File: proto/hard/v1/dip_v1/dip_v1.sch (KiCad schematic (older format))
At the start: 74 parts, among them J1 RJ12, J10 Conn_01x04_Female, J11 Conn_01x02_Male, J12 Conn_01x04_Female, J13 Conn_01x09_Male, J14 Conn_02x02_Counter_Clockwise, J2 RJ12, J3 RJ12, J4 RJ12, J5 Conn_01x04_Female, J6 RJ45, J7 AudioJack3, J8 Conn_01x04_Female, J9 Conn_01x05_Male, Q1 2N7000, Q2 2N7000, Q3 2N7000, Q4 BS250, Q5 BS250, Q6 2N7000, Q7 BS250, U1 BluePill, U2 LM339, U3 ST485EBDR, U4 74HC595, U5 ULN2803A, U6 74HC04, U7 LM358

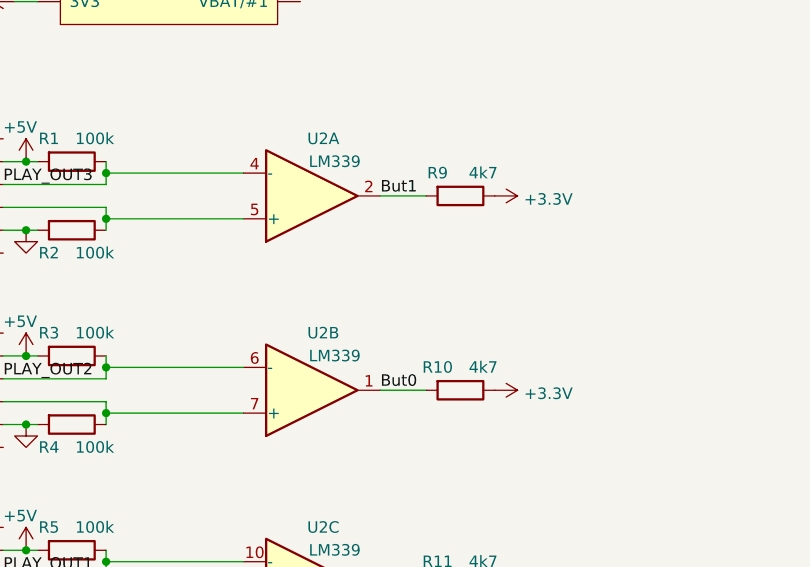
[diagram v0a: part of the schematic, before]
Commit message: Added example project with button connection schematic only. Corrected "dip" pins assignment to comply with main project.
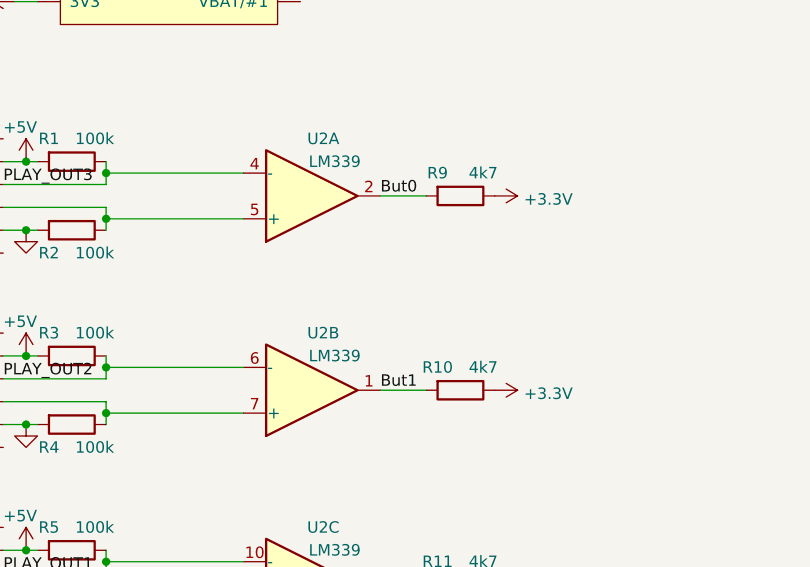
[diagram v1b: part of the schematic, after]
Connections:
- net But0: now also R9.2, U2.2; no longer R10.2, U2.1
- net But1: now also R10.2, U2.1; no longer R9.2, U2.2
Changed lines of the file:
@@
 EESchema Schematic File Version 4
-LIBS:dip_v1-cache
 EELAYER 29 0
 EELAYER END
@@
 Wire Wire Line
 	1900 3650 1900 3700
-Text Label 3100 3550 0    50   ~ 0
+Text Label 3100 4400 0    50   ~ 0
 But1
 Text Label 3100 5250 0    50   ~ 0
@@
 Text Label 3100 6100 0    50   ~ 0
 But3
-Text Label 3100 4400 0    50   ~ 0
+Text Label 3100 3550 0    50   ~ 0
 But0
 Text Label 1600 800  2    50   ~ 0
